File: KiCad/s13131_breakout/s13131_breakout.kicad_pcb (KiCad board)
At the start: 2 copper layers, 33 x 25.4 mm, 1 part

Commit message: Updated breakout.
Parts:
- removed S13131: ~, FWS:s13131-1536
- added C1: 1uF, Capacitor_SMD:C_0805_2012Metric, F.Cu at (43.0, 60.5)
- added J1: Conn_01x07_Pin, Connector_PinHeader_2.54mm:PinHeader_1x07_P2.54mm_Vertical, F.Cu at (27.9, 50.8)
- added S1: ~, FWS:s13131-1536, F.Cu at (43.2, 55.9)

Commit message: Updated breakout pcb.
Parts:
- moved S1 4.12 mm to (47.3, 55.9)
- moved C1 4.03 mm to (47.0, 61.0)
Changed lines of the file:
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@@
   )
   (footprint "FWS:s13131-1536" (layer "F.Cu")
-    (at 43.18 55.88)
+    (at 47.3 55.88)
     (property "Reference" "S1" (at 0 -5.08 0 unlocked) (layer "F.SilkS")
       (effects (font (size 1 1) (thickness 0.1)))
@@
   )
   (footprint "Capacitor_SMD:C_0805_2012Metric" (layer "F.Cu")
-    (at 43.05 60.5)
+    (at 47.05 61)
     (descr "Capacitor SMD 0805 (2012 Metric), square (rectangular) end terminal, IPC_7351 nominal, (Body size source: IPC-SM-782 page 76, https://www.pcb-3d.com/wordpress/wp-content/uploads/ipc-sm-782a_amendment_1_and_2.pdf, https://docs.google.com/spreadsheets/d/1BsfQQcO9C6DZCsRaXUlFlo91Tg2WpOkGARC1WS5S8t0/edit?usp=sharing), generated with kicad-footprint-generator")
     (tags "capacitor")

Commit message: Updated breakout pcb.
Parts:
- moved S1 2.39 mm to (46.0, 57.9)
- moved C1 1.61 mm to (46.1, 62.3)
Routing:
- net +3.3V: track 0.00 -> 23.2 mm
- net /CLK: track 0.00 -> 15.6 mm
- net Net-(S1-Vcp): track 0.00 -> 4.05 mm
- net GND: track 0.00 -> 3.97 mm
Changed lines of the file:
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@@
       (effects (font (size 1.27 1.27)))
     )
-    (property ki_fp_filters "Connector*:*_1x??_*")
-    (sheetfile "s13131_breakout.kicad_sch")
     (attr through_hole)
     (fp_line (start -1.33 -1.33) (end 0 -1.33)
@@
   )
   (footprint "FWS:s13131-1536" (layer "F.Cu")
-    (at 47.3 55.88)
+    (at 46 57.88)
     (property "Reference" "S1" (at 0 -5.08 0 unlocked) (layer "F.SilkS")
       (effects (font (size 1 1) (thickness 0.1)))
@@
       (effects (font (size 1 1) (thickness 0.15)))
     )
-    (sheetfile "s13131_breakout.kicad_sch")
     (attr smd)
     (fp_rect (start -4.65 -1.3) (end 4.65 1.3)
       (stroke (width 0.1) (type default)) (fill none) (layer "F.SilkS"))
+    (fp_line (start -4.224 0.63) (end 4.224 0.63)
+      (stroke (width 0.1) (type default)) (layer "F.Fab"))
     (fp_text user "${REFERENCE}" (at -2.54 7.62 0 unlocked) (layer "F.Fab")
       (effects (font (size 1 1) (thickness 0.15)))
@@
   )
   (footprint "Capacitor_SMD:C_0805_2012Metric" (layer "F.Cu")
-    (at 47.05 61)
+    (at 46.1 62.3)
     (descr "Capacitor SMD 0805 (2012 Metric), square (rectangular) end terminal, IPC_7351 nominal, (Body size source: IPC-SM-782 page 76, https://www.pcb-3d.com/wordpress/wp-content/uploads/ipc-sm-782a_amendment_1_and_2.pdf, https://docs.google.com/spreadsheets/d/1BsfQQcO9C6DZCsRaXUlFlo91Tg2WpOkGARC1WS5S8t0/edit?usp=sharing), generated with kicad-footprint-generator")
     (tags "capacitor")
@@
       (effects (font (size 1.27 1.27)))
     )
-    (property ki_fp_filters "C_*")
-    (sheetfile "s13131_breakout.kicad_sch")
     (attr smd)
     (fp_line (start -0.261252 -0.735) (end 0.261252 -0.735)
@@
   (gr_rect (start 25.4 45.72) (end 58.42 71.12)
     (stroke (width 0.1) (type default)) (fill none) (layer "Edge.Cuts"))
+  (gr_rect (start 36 48.5) (end 56 68.5)
+    (stroke (width 0.1) (type default)) (fill none) (layer "F.Fab"))
+  (gr_line (start 56 48.5) (end 36 68.5)
+    (stroke (width 0.1) (type default)) (layer "F.Fab"))
+  (gr_line (start 36 48.5) (end 56 68.5)
+    (stroke (width 0.1) (type default)) (layer "F.Fab"))
+  (segment (start 32.3 58.6) (end 29.58 55.88) (width 0.25) (layer "F.Cu") (net 1))
+  (segment (start 29.58 55.88) (end 27.94 55.88) (width 0.25) (layer "F.Cu") (net 1))
+  (segment (start 42.4 58.6) (end 32.3 58.6) (width 0.25) (layer "F.Cu") (net 1))
+  (segment (start 44.3 59.4) (end 45.15 60.25) (width 0.25) (layer "F.Cu") (net 6))
+  (segment (start 44.3 58.6) (end 44.3 59.4) (width 0.25) (layer "F.Cu") (net 6))
+  (segment (start 45.15 60.25) (end 45.15 62.3) (width 0.25) (layer "F.Cu") (net 6))
+  (segment (start 27.94 50.8) (end 42.8 50.8) (width 0.25) (layer "F.Cu") (net 7))
+  (segment (start 42.8 50.8) (end 47.7 55.7) (width 0.25) (layer "F.Cu") (net 7))
+  (segment (start 47.7 55.7) (end 47.7 57.16) (width 0.25) (layer "F.Cu") (net 7))
+  (segment (start 47.7 59.6) (end 47.05 60.25) (width 0.25) (layer "F.Cu") (net 8))
+  (segment (start 47.05 60.25) (end 47.05 62.3) (width 0.25) (layer "F.Cu") (net 8))
+  (segment (start 47.7 58.6) (end 47.7 59.6) (width 0.25) (layer "F.Cu") (net 8))
 )

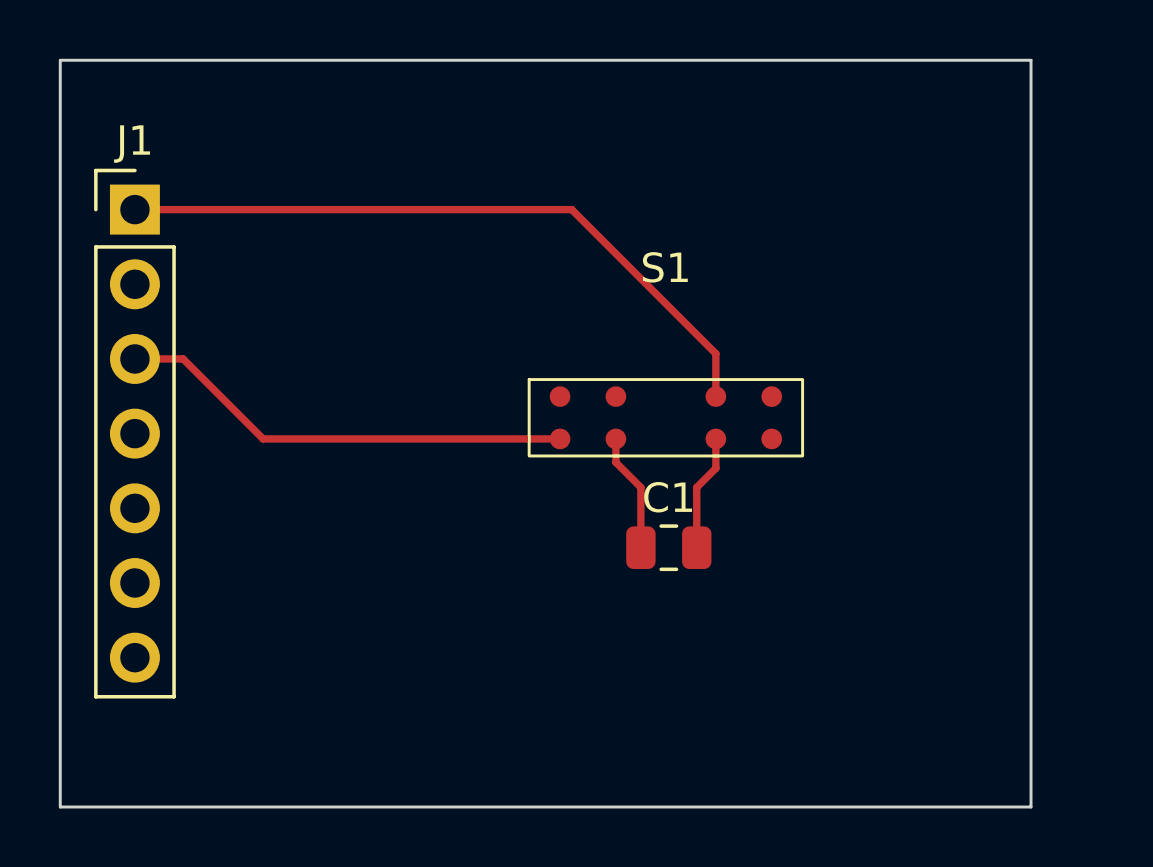
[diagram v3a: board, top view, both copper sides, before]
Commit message: Updated breakout board.
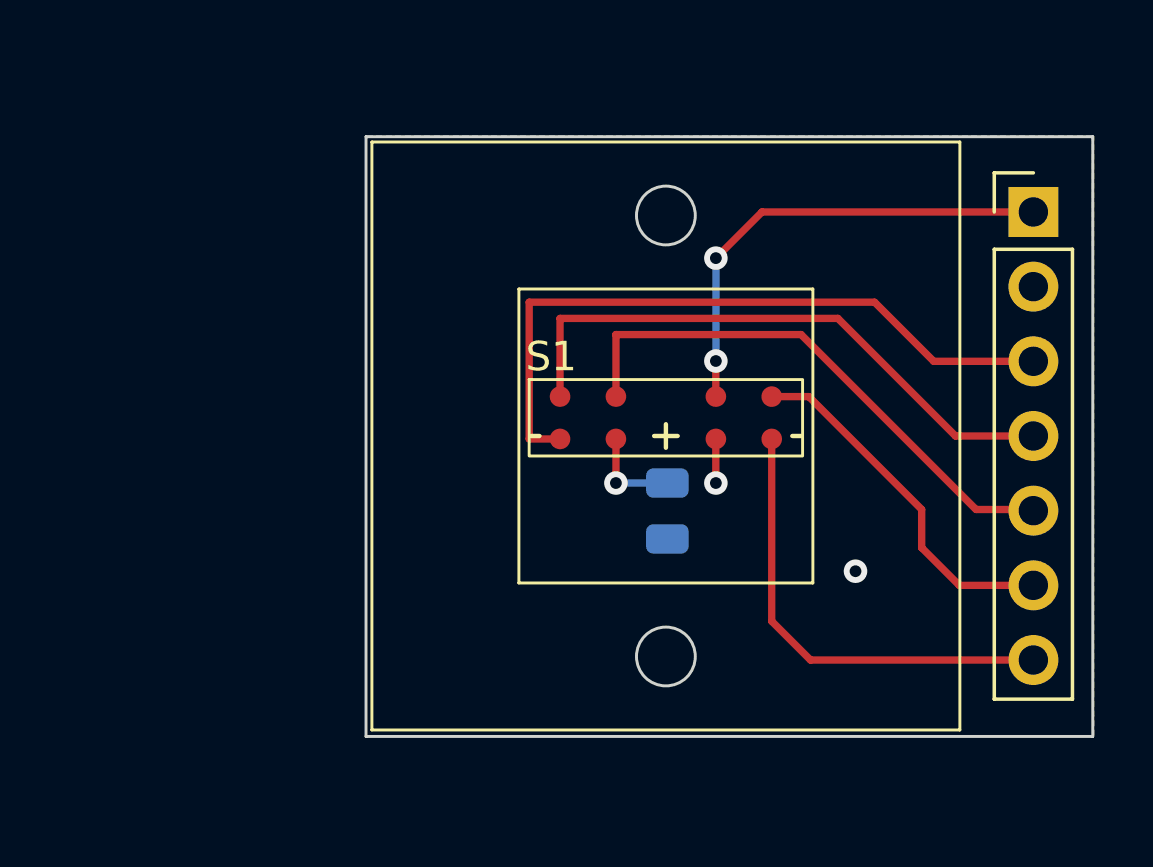
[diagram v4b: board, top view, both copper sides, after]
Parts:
- C1: moved to B.Cu
- moved J1 30.6 mm to (58.5, 50.9)
- moved C1 1.25 mm to (46.0, 61.0), turned to -90 degrees
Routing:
- net /ST: track 0.00 -> 20.4 mm
- net /Trig: track 0.00 -> 18.8 mm
- net /Video: track 0.00 -> 15.6 mm
- net /EOS: track 0.00 -> 12.3 mm
- net /CLK: track 15.6 -> 23.7 mm
- net +3.3V: track 23.2 -> 16.2 mm, vias 0 -> 2
- net GND: track 3.97 -> 1.50 mm, vias 0 -> 2
- net Net-(S1-Vcp): track 4.05 -> 3.25 mm, vias 0 -> 1
- added copper zone on B.Cu, net GND
- added copper zone on F.Cu, net GND
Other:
- board size 33 x 25.4 mm -> 24.7 x 20.4 mm
